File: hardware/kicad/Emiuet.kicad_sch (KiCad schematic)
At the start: 261 parts, among them J1 USB_C_Receptacle_USB2.0_16P, J2 USB_C_Receptacle_USB2.0_16P, J3 AudioJack3, J4 Conn_01x02_Pin, Q1 S9013 J3, SW1 SW_Slide_DPDT, SW1_0 Switch_SW_Push, SW1_1 Switch_SW_Push, SW1_10 Switch_SW_Push, SW1_11 Switch_SW_Push, SW1_12 Switch_SW_Push, SW1_2 Switch_SW_Push, SW1_3 Switch_SW_Push, SW1_4 Switch_SW_Push, SW1_5 Switch_SW_Push, SW1_6 Switch_SW_Push, SW1_7 Switch_SW_Push, SW1_8 Switch_SW_Push, SW1_9 Switch_SW_Push, SW2 SW_SPST, SW2_0 Switch_SW_Push, SW2_1 Switch_SW_Push, SW2_10 Switch_SW_Push, SW2_11 Switch_SW_Push, SW2_12 Switch_SW_Push, SW2_2 Switch_SW_Push, SW2_3 Switch_SW_Push, SW2_4 Switch_SW_Push, SW2_5 Switch_SW_Push, SW2_6 Switch_SW_Push, SW2_7 Switch_SW_Push, SW2_8 Switch_SW_Push, SW2_9 Switch_SW_Push, SW3 SW_SPST, SW3_0 Switch_SW_Push, SW3_1 Switch_SW_Push, SW3_10 Switch_SW_Push, SW3_11 Switch_SW_Push, SW3_12 Switch_SW_Push, SW3_2 Switch_SW_Push, SW3_3 Switch_SW_Push, SW3_4 Switch_SW_Push, SW3_5 Switch_SW_Push, SW3_6 Switch_SW_Push, SW3_7 Switch_SW_Push, SW3_8 Switch_SW_Push, SW3_9 Switch_SW_Push, SW4 SW_SPST, SW4_0 Switch_SW_Push, SW4_1 Switch_SW_Push, SW4_10 Switch_SW_Push, SW4_11 Switch_SW_Push, SW4_12 Switch_SW_Push, SW4_2 Switch_SW_Push, SW4_3 Switch_SW_Push, SW4_4 Switch_SW_Push, SW4_5 Switch_SW_Push, SW4_6 Switch_SW_Push, SW4_7 Switch_SW_Push, SW4_8 Switch_SW_Push, SW4_9 Switch_SW_Push, SW5_0 Switch_SW_Push, SW5_1 Switch_SW_Push, SW5_10 Switch_SW_Push, SW5_11 Switch_SW_Push, SW5_12 Switch_SW_Push, SW5_2 Switch_SW_Push, SW5_3 Switch_SW_Push, SW5_4 Switch_SW_Push, SW5_5 Switch_SW_Push, SW5_6 Switch_SW_Push, SW5_7 Switch_SW_Push, SW5_8 Switch_SW_Push, SW5_9 Switch_SW_Push, SW6_0 Switch_SW_Push, SW6_1 Switch_SW_Push, SW6_10 Switch_SW_Push, SW6_11 Switch_SW_Push, SW6_12 Switch_SW_Push, SW6_2 Switch_SW_Push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

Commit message: Fix Kicad Data
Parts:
- removed JP1: Jumper_2_Bridged, TestPoint:TestPoint_2Pads_Pitch2.54mm_Drill0.8mm, symbol Jumper:Jumper_2_Bridged
- removed JP3: Jumper_2_Bridged, Jumper:SolderJumper-2_P1.3mm_Bridged_RoundedPad1.0x1.5mm, symbol Jumper:Jumper_2_Bridged
- BT1: footprint EUB_Passives:Battery Cell 800mah bis -> EUB_Passives:Battery Cell 800mah nobis
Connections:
- net USB1_VBUS: now also C21.1, C22.1, U7.13 (IN)
- net at U7.1 (TS): now also TH1.1
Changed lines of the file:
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@@
 	(wire
 		(pts
-			(xy 271.78 204.47) (xy 278.13 204.47)
+			(xy 271.78 204.47) (xy 293.37 204.47)
 		)
 		(stroke
@@
 	(wire
 		(pts
-			(xy 306.07 232.41) (xy 313.69 232.41)
+			(xy 306.07 232.41) (xy 349.25 232.41)
 		)
 		(stroke
@@
 	(wire
 		(pts
-			(xy 288.29 204.47) (xy 293.37 204.47)
-		)
-		(stroke
-			(width 0)
-			(type default)
-		)
-	)
-	(wire
-		(pts
 			(xy 374.65 241.3) (xy 375.92 241.3)
 		)
@@
 	(wire
 		(pts
-			(xy 323.85 232.41) (xy 349.25 232.41)
-		)
-		(stroke
-			(width 0)
-			(type default)
-		)
-	)
-	(wire
-		(pts
 			(xy 318.77 66.04) (xy 318.77 69.85)
 		)
@@
 	)
 	(symbol
-		(lib_id "Jumper:Jumper_2_Bridged")
-		(at 318.77 232.41 0)
-		(unit 1)
-		(exclude_from_sim no)
-		(in_bom yes)
-		(on_board yes)
-		(dnp no)
-		(fields_autoplaced yes)
-		(property "Reference" "JP3"
-			(at 318.77 227.33 0)
-			(effects
-				(font
-					(size 1.27 1.27)
-				)
-			)
-		)
-		(property "Value" "Jumper_2_Bridged"
-			(at 318.77 229.87 0)
-			(effects
-				(font
-					(size 1.27 1.27)
-				)
-			)
-		)
-		(property "Footprint" "Jumper:SolderJumper-2_P1.3mm_Bridged_RoundedPad1.0x1.5mm"
-			(at 318.77 232.41 0)
-			(effects
-				(font
-					(size 1.27 1.27)
-				)
-				(hide yes)
-			)
-		)
-		(property "Datasheet" "~"
-			(at 318.77 232.41 0)
-			(effects
-				(font
-					(size 1.27 1.27)
-				)
-				(hide yes)
-			)
-		)
-		(property "Description" "Jumper, 2-pole, closed/bridged"
-			(at 318.77 232.41 0)
-			(effects
-				(font
-					(size 1.27 1.27)
-				)
-				(hide yes)
-			)
-		)
-		(pin "1"
-		)
-		(pin "2"
-		)
-		(instances
-			(project ""
-				(path "/c9191c2a-649b-4f9d-b8cd-0f4c3bb1b88c"
-					(reference "JP3")
-					(unit 1)
-				)
-			)
-		)
-	)
-	(symbol
 		(lib_name "D_Small_1")
 		(lib_id "Device:D_Small")
@@
 	)
 	(symbol
-		(lib_id "Jumper:Jumper_2_Bridged")
-		(at 283.21 204.47 0)
-		(unit 1)
-		(exclude_from_sim no)
-		(in_bom yes)
-		(on_board yes)
-		(dnp no)
-		(property "Reference" "JP1"
-			(at 283.21 199.39 0)
-			(effects
-				(font
-					(size 1.27 1.27)
-				)
-			)
-		)
-		(property "Value" "Jumper_2_Bridged"
-			(at 283.718 201.93 0)
-			(effects
-				(font
-					(size 1.27 1.27)
-				)
-			)
-		)
-		(property "Footprint" "TestPoint:TestPoint_2Pads_Pitch2.54mm_Drill0.8mm"
-			(at 283.21 204.47 0)
-			(effects
-				(font
-					(size 1.27 1.27)
-				)
-				(hide yes)
-			)
-		)
-		(property "Datasheet" "~"
-			(at 283.21 204.47 0)
-			(effects
-				(font
-					(size 1.27 1.27)
-				)
-				(hide yes)
-			)
-		)
-		(property "Description" "Jumper, 2-pole, closed/bridged"
-			(at 283.21 204.47 0)
-			(effects
-				(font
-					(size 1.27 1.27)
-				)
-				(hide yes)
-			)
-		)
-		(pin "2"
-		)
-		(pin "1"
-		)
-		(instances
-			(project ""
-				(path "/c9191c2a-649b-4f9d-b8cd-0f4c3bb1b88c"
-					(reference "JP1")
-					(unit 1)
-				)
-			)
-		)
-	)
-	(symbol
 		(lib_id "power:GNDA")
 		(at 345.44 149.86 0)
@@
 			)
 		)
-		(property "Footprint" "EUB_Passives:Battery Cell 800mah bis"
+		(property "Footprint" "EUB_Passives:Battery Cell 800mah nobis"
 			(at 386.08 223.52 0)
 			(effects

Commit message: KiCad REV-B Design
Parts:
- added C31: 1μ, EUB_Passives:C_0603_1608Metric_noSilks, symbol Device:C_Small
- added R6: 10k, EUB_Passives:R_0603_1608Metric_noSilks, symbol Device:R_Small_US
- added R7: JP_TX0, EUB_Passives:R_0603_1608Metric_noSilks, symbol Device:R_Small_US
- added R8: JP_RX0, EUB_Passives:R_0603_1608Metric_noSilks, symbol Device:R_Small_US
- added SW5: SW_SPST, Button_Switch_SMD:SW_SPST_TS-1088-xR020, symbol Switch:SW_SPST
- added TP1, TP2, TP3, TP4, TP5: TestPoint, TestPoint:TestPoint_Pad_D1.0mm, symbol Connector:TestPoint
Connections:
- net +3V3: now also R6.2, TP1.1
- net GNDD: now also C31.1, SW5.2 (B), TP2.1, TP4.1
- net SW_LEFT: now also R8.2; no longer U1.40 (RXD0)
- net TXD: now also R7.1; no longer U1.39 (TXD0)
- net at R1.1, U1.45 (EN): now also C31.2, SW5.1 (A)
- net BOOT: now reaches U1.4 (IO0)
- net BOOT: now also R6.1
- new net: R8.1, TP5.1, U1.40 (RXD0)
- new net: R7.2, TP3.1, U1.39 (TXD0)
- no-connect marks 21 -> 20
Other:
- moved on the sheet: C1, C21, C22, R1

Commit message: DEV-Aでテストしながら基板の改良
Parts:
- removed TP2: TestPoint, TestPoint:TestPoint_Pad_D1.0mm, symbol Connector:TestPoint
- added R30: 100k, EUB_Passives:R_0603_1608Metric_noSilks, symbol Device:R_Small_US
- added SW6: SW_SPST, Button_Switch_SMD:SW_SPST_TS-1088-xR020, symbol Switch:SW_SPST
- added SW7, SW8: SW_SPDT, Button_Switch_SMD:SW_SPDT_Shouhan_MSK12C02, symbol Switch:SW_SPDT
- R7: value JP_TX0 -> 470
- R8: value JP_RX0 -> 470
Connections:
- net +3V3: now also SW6.1 (A); no longer TP1.1
- net GNDD: now also TP1.1, R30.1, SW6.2 (B)
- net SW_LEFT: now also SW8.3 (C); no longer R8.2
- net TXD: now also SW7.3 (C); no longer R7.1
- net FLASH_RX: now reaches R8.1, U1.40 (RXD0)
- net FLASH_RX: no longer TP5.1
- net FLASH_TX: now reaches R7.2, U1.39 (TXD0)
- net FLASH_TX: no longer TP3.1
- net at Q1.1 (B), R4.2: now also R30.2
- new net: SW8.1 (A), TP5.1
- new net: R7.1, SW7.2 (B)
- new net: R8.2, SW8.2 (B)
- new net: SW7.1 (A), TP3.1
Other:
- note added: "FLAS用UART確保"
- moved on the sheet: D3, R5, R7, R8, SW1, TP3, TP4, TP5

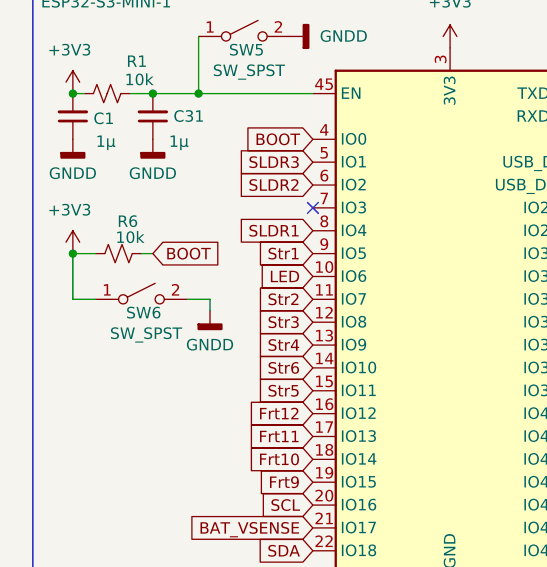
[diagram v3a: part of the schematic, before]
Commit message: BOOTスイッチ修正
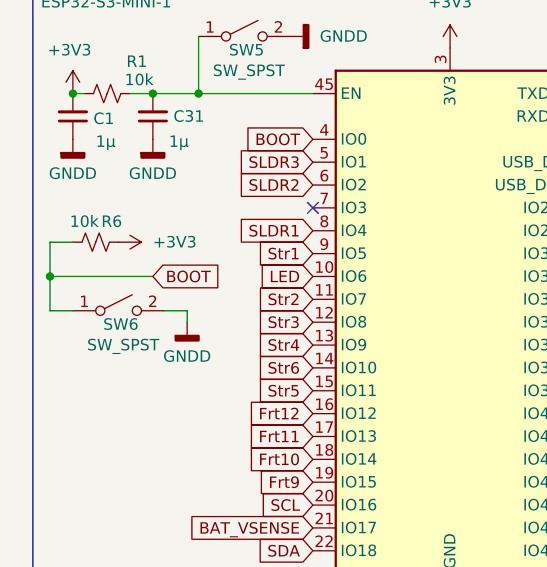
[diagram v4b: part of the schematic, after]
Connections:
- net +3V3: no longer SW6.1 (A)
- net BOOT: now also SW6.1 (A)
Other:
- moved on the sheet: R6, SW6
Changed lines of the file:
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@@
 	)
 	(junction
-		(at 21.59 50.8)
-		(diameter 0)
-		(color 0 0 0 0)
-	)
-	(junction
 		(at 383.54 146.05)
 		(diameter 0)
@@
 	)
 	(junction
+		(at 19.05 53.34)
+		(diameter 0)
+		(color 0 0 0 0)
+	)
+	(junction
 		(at 201.93 77.47)
 		(diameter 0)
@@
 	(wire
 		(pts
-			(xy 21.59 50.8) (xy 21.59 55.88)
-		)
-		(stroke
-			(width 0)
-			(type default)
-		)
-	)
-	(wire
-		(pts
 			(xy 237.49 77.47) (xy 237.49 81.28)
 		)
@@
 	(wire
 		(pts
-			(xy 36.83 55.88) (xy 36.83 57.15)
+			(xy 34.29 57.15) (xy 34.29 58.42)
 		)
 		(stroke
@@
 	(wire
 		(pts
+			(xy 19.05 53.34) (xy 30.48 53.34)
+		)
+		(stroke
+			(width 0)
+			(type default)
+		)
+	)
+	(wire
+		(pts
 			(xy 194.31 95.25) (xy 194.31 99.06)
 		)
@@
 	(wire
 		(pts
+			(xy 19.05 49.53) (xy 21.59 49.53)
+		)
+		(stroke
+			(width 0)
+			(type default)
+		)
+	)
+	(wire
+		(pts
 			(xy 124.46 77.47) (xy 130.81 77.47)
 		)
@@
 	(wire
 		(pts
-			(xy 21.59 50.8) (xy 24.13 50.8)
-		)
-		(stroke
-			(width 0)
-			(type default)
-		)
-	)
-	(wire
-		(pts
 			(xy 241.3 135.89) (xy 241.3 138.43)
 		)
@@
 	(wire
 		(pts
+			(xy 19.05 53.34) (xy 19.05 57.15)
+		)
+		(stroke
+			(width 0)
+			(type default)
+		)
+	)
+	(wire
+		(pts
 			(xy 139.7 264.16) (xy 137.16 264.16)
 		)
@@
 	(wire
 		(pts
-			(xy 21.59 55.88) (xy 24.13 55.88)
+			(xy 19.05 57.15) (xy 21.59 57.15)
 		)
 		(stroke
@@
 	(wire
 		(pts
+			(xy 19.05 49.53) (xy 19.05 53.34)
+		)
+		(stroke
+			(width 0)
+			(type default)
+		)
+	)
+	(wire
+		(pts
 			(xy 273.05 62.23) (xy 290.83 62.23)
 		)
@@
 	(wire
 		(pts
-			(xy 29.21 50.8) (xy 30.48 50.8)
-		)
-		(stroke
-			(width 0)
-			(type default)
-		)
-	)
-	(wire
-		(pts
 			(xy 273.05 91.44) (xy 290.83 91.44)
 		)
@@
 	(wire
 		(pts
-			(xy 34.29 55.88) (xy 36.83 55.88)
+			(xy 31.75 57.15) (xy 34.29 57.15)
 		)
 		(stroke
@@
 	(global_label "BOOT"
 		(shape input)
-		(at 30.48 50.8 0)
+		(at 30.48 53.34 0)
 		(fields_autoplaced yes)
 		(effects
@@
 		)
 		(property "Intersheetrefs" "${INTERSHEET_REFS}"
-			(at 38.3638 50.8 0)
+			(at 38.3638 53.34 0)
 			(effects
 				(font
@@
 	)
 	(symbol
+		(lib_id "power:+3V3")
+		(at 26.67 49.53 270)
+		(unit 1)
+		(exclude_from_sim no)
+		(in_bom yes)
+		(on_board yes)
+		(dnp no)
+		(fields_autoplaced yes)
+		(property "Reference" "#PWR031"
+			(at 22.86 49.53 0)
+			(effects
+				(font
+					(size 1.27 1.27)
+				)
+				(hide yes)
+			)
+		)
+		(property "Value" "+3V3"
+			(at 30.48 49.5299 90)
+			(effects
+				(font
+					(size 1.27 1.27)
+				)
+				(justify left)
+			)
+		)
+		(property "Footprint" ""
+			(at 26.67 49.53 0)
+			(effects
+				(font
+					(size 1.27 1.27)
+				)
+				(hide yes)
+			)
+		)
+		(property "Datasheet" ""
+			(at 26.67 49.53 0)
+			(effects
+				(font
+					(size 1.27 1.27)
+				)
+				(hide yes)
+			)
+		)
+		(property "Description" "Power symbol creates a global label with name \"+3V3\""
+			(at 26.67 49.53 0)
+			(effects
+				(font
+					(size 1.27 1.27)
+				)
+				(hide yes)
+			)
+		)
+		(pin "1"
+		)
+		(instances
+			(project "Emiuet"
+				(path "/c9191c2a-649b-4f9d-b8cd-0f4c3bb1b88c"
+					(reference "#PWR031")
+					(unit 1)
+				)
+			)
+		)
+	)
+	(symbol
 		(lib_name "D_Small_1")
 		(lib_id "Device:D_Small")
@@
 	(symbol
 		(lib_id "Switch:SW_SPST")
-		(at 29.21 55.88 0)
+		(at 26.67 57.15 0)
 		(unit 1)
 		(exclude_from_sim no)
@@
 		(dnp no)
 		(property "Reference" "SW6"
-			(at 29.464 57.404 0)
+			(at 26.924 58.674 0)
 			(effects
 				(font
@@
 		)
 		(property "Value" "SW_SPST"
-			(at 29.718 59.69 0)
+			(at 27.178 60.96 0)
 			(effects
 				(font
@@
 		)
 		(property "Footprint" "Button_Switch_SMD:SW_SPST_TS-1088-xR020"
-			(at 29.21 55.88 0)
+			(at 26.67 57.15 0)
 			(effects
 				(font
@@
 		)
 		(property "Datasheet" "~"
-			(at 29.21 55.88 0)
+			(at 26.67 57.15 0)
 			(effects
 				(font
@@
 		)
 		(property "Description" "Single Pole Single Throw (SPST) switch"
-			(at 29.21 55.88 0)
+			(at 26.67 57.15 0)
 			(effects
 				(font
@@
 	(symbol
 		(lib_id "power:GNDD")
-		(at 36.83 57.15 0)
+		(at 34.29 58.42 0)
 		(unit 1)
 		(exclude_from_sim no)
@@
 		(fields_autoplaced yes)
 		(property "Reference" "#PWR030"
-			(at 36.83 63.5 0)
+			(at 34.29 64.77 0)
 			(effects
 				(font
@@
 		)
 		(property "Value" "GNDD"
-			(at 36.83 60.96 0)
+			(at 34.29 62.23 0)
 			(effects
 				(font
@@
 		)
 		(property "Footprint" ""
-			(at 36.83 57.15 0)
+			(at 34.29 58.42 0)
 			(effects
 				(font
@@
 		)
 		(property "Datasheet" ""
-			(at 36.83 57.15 0)
+			(at 34.29 58.42 0)
 			(effects
 				(font
@@
 		)
 		(property "Description" "Power symbol creates a global label with name \"GNDD\" , digital ground"
-			(at 36.83 57.15 0)
+			(at 34.29 58.42 0)
 			(effects
 				(font
@@
 	)
 	(symbol
-		(lib_id "power:+3V3")
-		(at 21.59 50.8 0)
-		(unit 1)
-		(exclude_from_sim no)
-		(in_bom yes)
-		(on_board yes)
-		(dnp no)
-		(property "Reference" "#PWR031"
-			(at 21.59 54.61 0)
-			(effects
-				(font
-					(size 1.27 1.27)
-				)
-				(hide yes)
-			)
-		)
-		(property "Value" "+3V3"
-			(at 18.796 45.974 0)
-			(effects
-				(font
-					(size 1.27 1.27)
-				)
-				(justify left)
-			)
-		)
-		(property "Footprint" ""
-			(at 21.59 50.8 0)
-			(effects
-				(font
-					(size 1.27 1.27)
-				)
-				(hide yes)
-			)
-		)
-		(property "Datasheet" ""
-			(at 21.59 50.8 0)
-			(effects
-				(font
-					(size 1.27 1.27)
-				)
-				(hide yes)
-			)
-		)
-		(property "Description" "Power symbol creates a global label with name \"+3V3\""
-			(at 21.59 50.8 0)
-			(effects
-				(font
-					(size 1.27 1.27)
-				)
-				(hide yes)
-			)
-		)
-		(pin "1"
-		)
-		(instances
-			(project "Emiuet"
-				(path "/c9191c2a-649b-4f9d-b8cd-0f4c3bb1b88c"
-					(reference "#PWR031")
-					(unit 1)
-				)
-			)
-		)
-	)
-	(symbol
 		(lib_name "D_Small_1")
 		(lib_id "Device:D_Small")
@@
 	(symbol
 		(lib_id "Device:R_Small_US")
-		(at 26.67 50.8 270)
+		(at 24.13 49.53 90)
 		(unit 1)
 		(exclude_from_sim no)
@@
 		(dnp no)
 		(property "Reference" "R6"
-			(at 27.686 47.244 90)
+			(at 25.908 47.244 90)
 			(effects
 				(font
@@
 		)
 		(property "Value" "10k"
-			(at 27.94 49.022 90)
+			(at 22.86 47.244 90)
 			(effects
 				(font
@@
 		)
 		(property "Footprint" "EUB_Passives:R_0603_1608Metric_noSilks"
-			(at 26.67 50.8 0)
+			(at 24.13 49.53 0)
 			(effects
 				(font
@@
 		)
 		(property "Datasheet" "~"
-			(at 26.67 50.8 0)
+			(at 24.13 49.53 0)
 			(effects
 				(font
@@
 		)
 		(property "Description" "Resistor, small US symbol"
-			(at 26.67 50.8 0)
+			(at 24.13 49.53 0)
 			(effects
 				(font
